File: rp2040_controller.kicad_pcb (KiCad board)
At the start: 4 copper layers, 19 x 29.5 mm, 33 parts, among them J1 Conn_01x12, J2 Conn_01x15, J3 Conn_01x12, J4 Conn_01x05, J5 Conn_01x02, J6 Conn_01x02, U1 RP2040, U2 AP2112K-3.3, U3 W25Q64JV, Y1 XYDBPCNANF-12MHZ

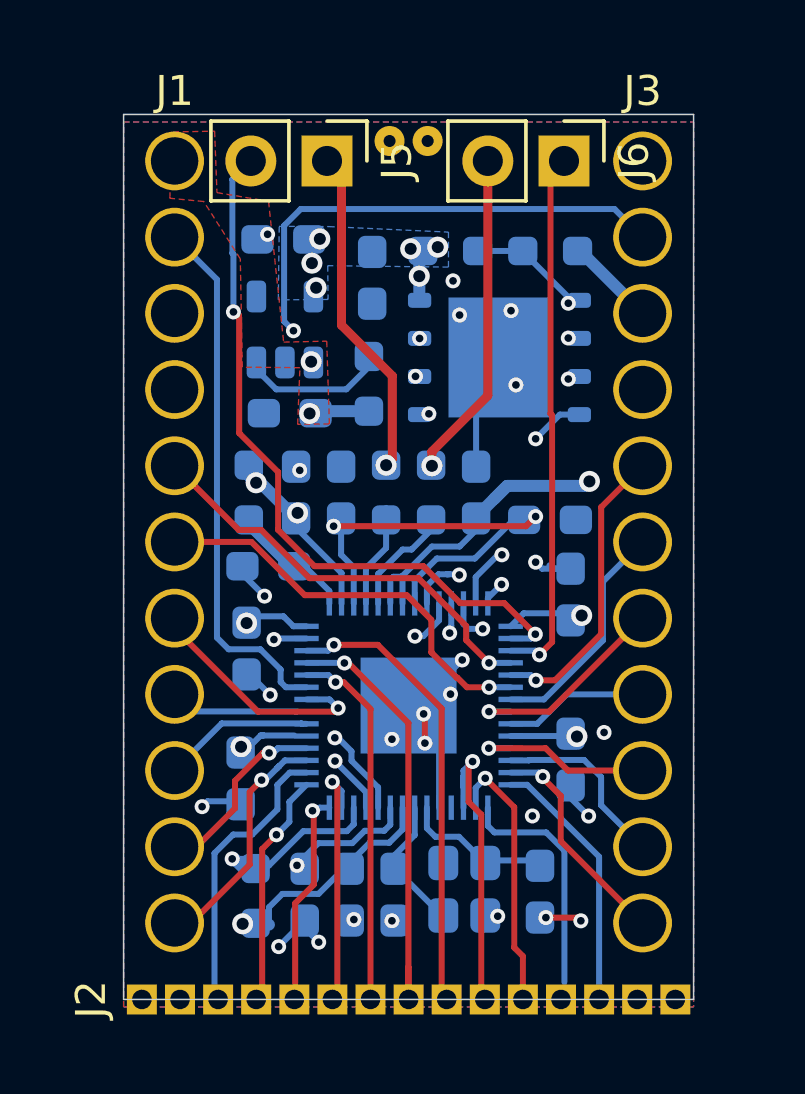
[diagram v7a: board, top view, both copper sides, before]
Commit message: top&bottom connect
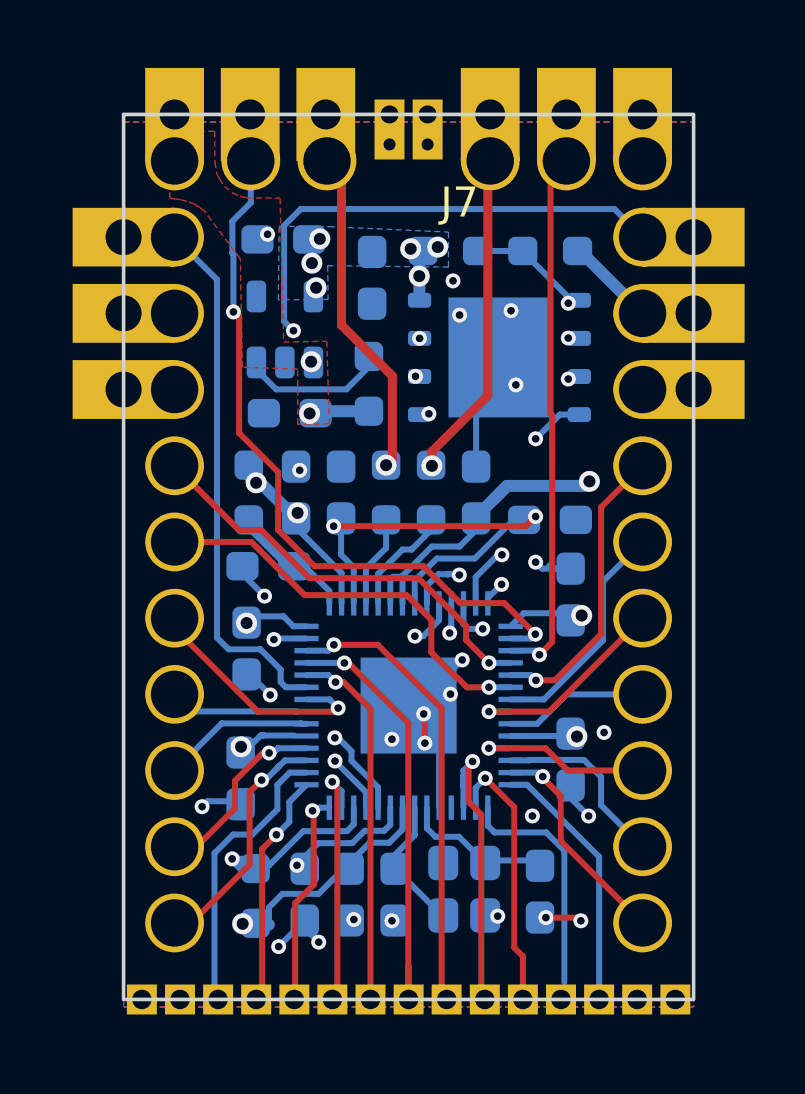
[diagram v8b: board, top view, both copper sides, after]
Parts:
- removed J1, J3: Conn_01x12, ec_parts:PinHeader_1x12_P2.54mm_Vertical
- removed J2: Conn_01x15, ec_parts:PinHeader_1x15_P1.27mm_Vertical
- removed J4: Conn_01x05, ec_parts:TestPinHeader_1x03_P1.27mm_Vertical
- removed J5, J6: Conn_01x02, Connector_PinHeader_2.54mm:PinHeader_1x02_P2.54mm_Vertical
- added J7: rp2040_controller, ec_parts:rp2040_controller, F.Cu at (100.0, 99.8)
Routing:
- net /USB_N: track 10.4 -> 11.1 mm
